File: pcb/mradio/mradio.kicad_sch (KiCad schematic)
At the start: 1 part, among them U1 STM32H745ZITx

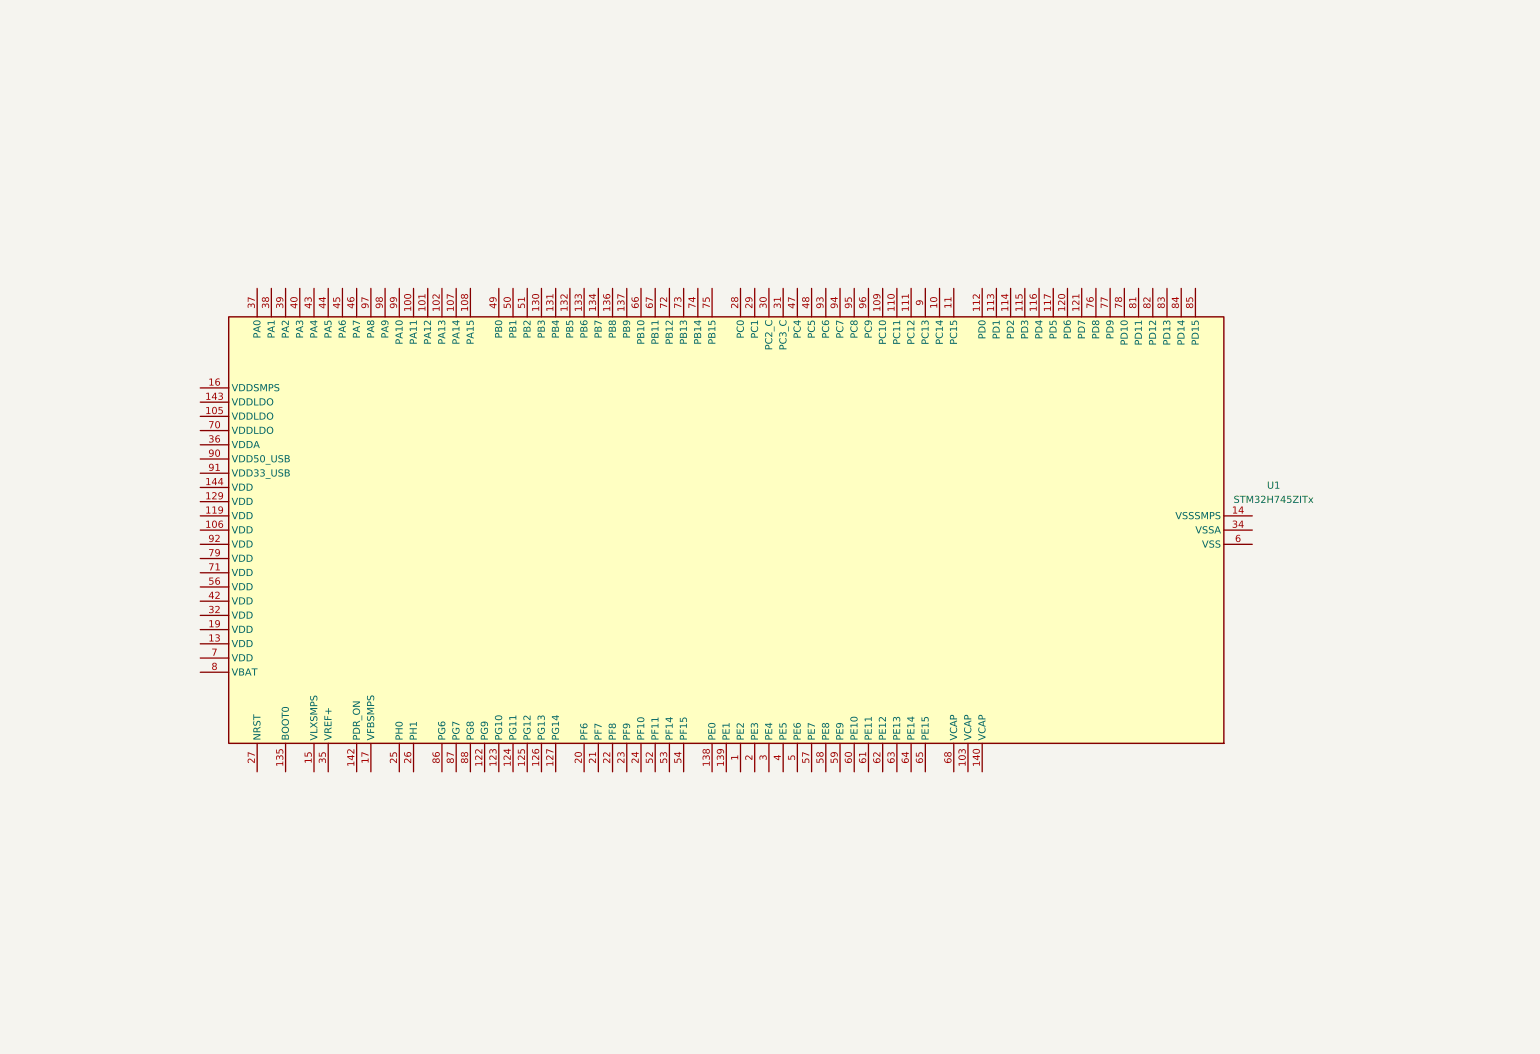
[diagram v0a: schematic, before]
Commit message: updated ioc and began mcu schematic
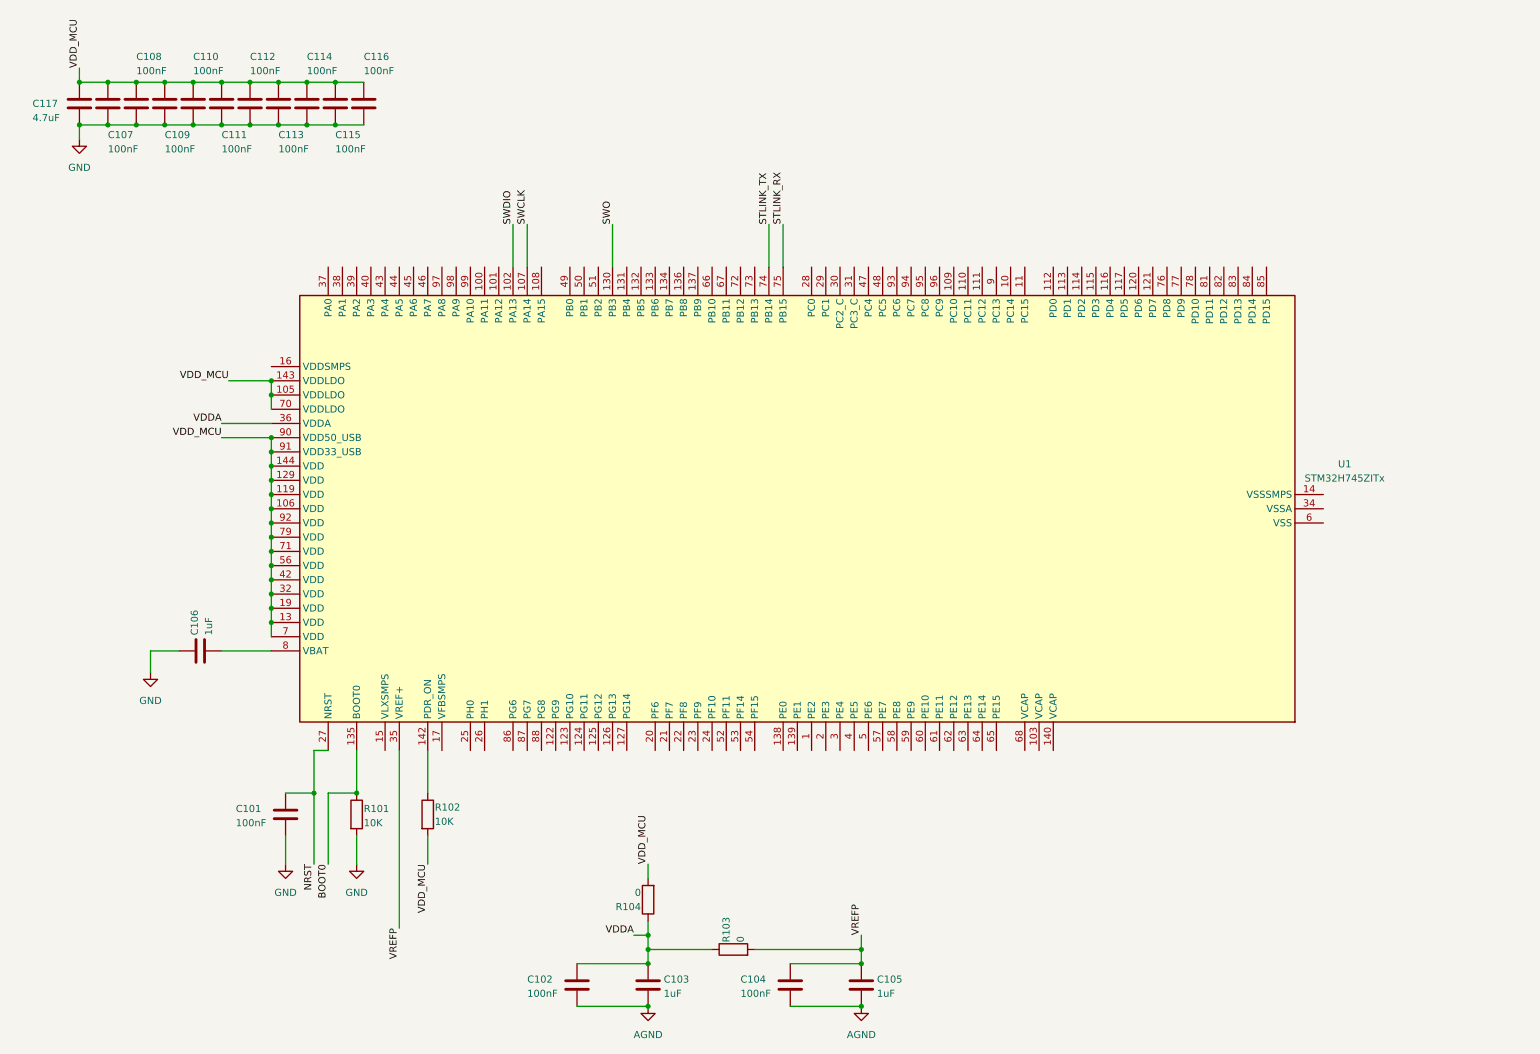
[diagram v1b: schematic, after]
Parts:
- added C101, C102, C104, C107, C108, C109, C110, C111, C112, C113, C114, C115, C116: 100nF, Capacitor_SMD:C_0603_1608Metric, symbol Device:C
- added C103, C105, C106: 1uF, Capacitor_SMD:C_0603_1608Metric, symbol Device:C
- added C117: 4.7uF, Capacitor_SMD:C_0603_1608Metric, symbol Device:C
- added R101, R102: 10K, Resistor_SMD:R_0603_1608Metric, symbol Device:R
- added R103, R104: 0, Resistor_SMD:R_0603_1608Metric, symbol Device:R
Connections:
- net SWDIO: now reaches U1.102 (PA13)
- net VDD_MCU: now reaches U1.105 (VDDLDO)
- net VDD_MCU: now also U1.106 (VDD), U1.119 (VDD), U1.129 (VDD), U1.13 (VDD), U1.143 (VDDLDO), U1.144 (VDD), U1.19 (VDD), U1.32 (VDD), U1.42 (VDD), U1.56 (VDD), U1.7 (VDD), U1.70 (VDDLDO), U1.71 (VDD), U1.79 (VDD), U1.90 (VDD50_USB), U1.91 (VDD33_USB), U1.92 (VDD), C107.1, C108.1, C109.1, C110.1, C111.1, C112.1, C113.1, C114.1, C115.1, C116.1, C117.1, R102.2, R104.2
- net SWCLK: now reaches U1.107 (PA14)
- net SWO: now reaches U1.130 (PB3)
- net BOOT0: now reaches U1.135 (BOOT0)
- net BOOT0: now also R101.1
- net at U1.142 (PDR_ON): now also R102.1
- net NRST: now reaches U1.27 (NRST)
- net NRST: now also C101.1
- net VREFP: now reaches U1.35 (VREF+)
- net VREFP: now also C104.1, C105.1, R103.2
- net VDDA: now reaches U1.36 (VDDA)
- net VDDA: now also C102.1, C103.1, R103.1, R104.1
- net STLINK_TX: now reaches U1.74 (PB14)
- net STLINK_RX: now reaches U1.75 (PB15)
- net at U1.8 (VBAT): now also C106.2
- new net AGND: C102.2, C103.2, C104.2, C105.2
- new net GND: C101.2, C106.1, C107.2, C108.2, C109.2, C110.2, C111.2, C112.2, C113.2, C114.2, C115.2, C116.2, C117.2, R101.2
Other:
- moved on the sheet: U1

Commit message: mcu schematic mostly done, need to get stlinkv3 header
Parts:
- added C118, C119: 2.2uF, Capacitor_SMD:C_0603_1608Metric, symbol Device:C
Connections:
- net AGND is gone; now on net GND: C102.2, C103.2, C104.2, C105.2
- net GND: now also U1.104 (VSS), U1.118 (VSS), U1.12 (VSS), U1.128 (VSS), U1.14 (VSSSMPS), U1.141 (VSS), U1.18 (VSS), U1.33 (VSS), U1.34 (VSSA), U1.41 (VSS), U1.55 (VSS), U1.6 (VSS), U1.69 (VSS), U1.80 (VSS), U1.89 (VSS), C118.2, C119.2
- net WM_RESET: now reaches U1.1 (PE2)
- net VCAP: now reaches U1.103 (VCAP)
- net VCAP: now also U1.140 (VCAP), U1.68 (VCAP), C118.1, C119.1
- net SDMMC1_D2: now reaches U1.109 (PC10)
- net SDMMC1_D3: now reaches U1.110 (PC11)
- net SDMMC1_CK: now reaches U1.111 (PC12)
- net SDMMC1_CMD: now reaches U1.114 (PD2)
- net WL_REG_ON: now reaches U1.120 (PD6)
- net WL_DEV_WAKE: now reaches U1.121 (PD7)
- net WL_HOST_WAKE: now reaches U1.122 (PG9)
- net SPI1_SCK: now reaches U1.124 (PG11)
- net SPI1_CS: now reaches U1.127 (PG14)
- net SPI1_MISO: now reaches U1.131 (PB4)
- net SPI1_MOSI: now reaches U1.132 (PB5)
- net SPI_INT: now reaches U1.133 (PB6)
- net WM_WAKE: now reaches U1.2 (PE3)
- net M4_DBG1: now reaches U1.21 (PF7)
- net M4_DBG2: now reaches U1.22 (PF8)
- net M7_DBG1: now reaches U1.23 (PF9)
- net M7_DBG2: now reaches U1.24 (PF10)
- net ETH_MDC: now reaches U1.29 (PC1)
- net WM_BUSY: now reaches U1.3 (PE4)
- net ETH_REF_CLK: now reaches U1.38 (PA1)
- net ETH_MDIO: now reaches U1.39 (PA2)
- net ETH_RESET: now reaches U1.43 (PA4)
- net ETH_INT: now reaches U1.44 (PA5)
- net ETH_CRS_DV: now reaches U1.46 (PA7)
- net ETH_RXD0: now reaches U1.47 (PC4)
- net ETH_RXD1: now reaches U1.48 (PC5)
- net ETH_TX_EN: now reaches U1.67 (PB11)
- net ETH_TXD0: now reaches U1.72 (PB12)
- net ETH_TXD1: now reaches U1.73 (PB13)
- net SoS_LED1: now reaches U1.85 (PD15)
- net SoS_LED2: now reaches U1.86 (PG6)
- net SoS_LED3: now reaches U1.87 (PG7)
- net SoS_LED4: now reaches U1.88 (PG8)
- net SDMMC1_D0: now reaches U1.95 (PC8)
- net SDMMC1_D1: now reaches U1.96 (PC9)
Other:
- moved on the sheet: C102, C103, C104, C105, C107, C108, C109, C110, C111, C112, C113, C114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

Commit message: finalized mcu schematic for review, using LDO-only mode and assuming 3.3V MCU input
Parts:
- removed C106: 1uF, Capacitor_SMD:C_0603_1608Metric, symbol Device:C
- added C120: 1uF, Capacitor_SMD:C_0603_1608Metric, symbol Device:C
- added D1, D2, D3, D4, D5, D6, D7, D8: LED, symbol Device:LED
- added R105, R106, R107, R108, R109, R110, R111, R112: 1K, Resistor_SMD:R_0603_1608Metric, symbol Device:R
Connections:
- net GND: now also C120.2, D1.1 (K), D2.1 (K), D3.1 (K), D4.1 (K), D5.1 (K), D6.1 (K), D7.1 (K), D8.1 (K)
- net M4_DBG1: now also R109.2
- net M4_DBG2: now also R110.2
- net M7_DBG1: now also R111.2
- net M7_DBG2: now also R112.2
- net SoS_LED1: now also R105.2
- net SoS_LED2: now also R106.2
- net SoS_LED3: now also R107.2
- net SoS_LED4: now also R108.2
- net VDD_MCU: now also U1.8 (VBAT), C120.1; no longer U1.106 (VDD), U1.119 (VDD), U1.129 (VDD), U1.13 (VDD), U1.144 (VDD), U1.19 (VDD), U1.32 (VDD), U1.42 (VDD), U1.56 (VDD), U1.7 (VDD), U1.71 (VDD), U1.79 (VDD), U1.90 (VDD50_USB), U1.91 (VDD33_USB), U1.92 (VDD)
- new net: U1.106 (VDD), U1.119 (VDD), U1.129 (VDD), U1.13 (VDD), U1.144 (VDD), U1.19 (VDD), U1.32 (VDD), U1.42 (VDD), U1.56 (VDD), U1.7 (VDD), U1.71 (VDD), U1.79 (VDD), U1.92 (VDD)
- new net: D5.2 (A), R109.1
- new net: D1.2 (A), R105.1
- new net: D8.2 (A), R112.1
- new net: D7.2 (A), R111.1
- new net: D3.2 (A), R107.1
- new net: D2.2 (A), R106.1
- new net: D4.2 (A), R108.1
- new net: D6.2 (A), R110.1
- new net 3v3_LDO_OUT: U1.90 (VDD50_USB), U1.91 (VDD33_USB)
